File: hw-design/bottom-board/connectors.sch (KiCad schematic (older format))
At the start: 17 parts, among them J1 JACK_TRS_6PINS, J2 JACK_TRS_6PINS, J3 JACK_TRS_6PINS, J4 JACK_TRS_6PINS, J5 JACK_TRS_6PINS, J6 RJ45_LEDS, P5 BARREL_JACK, P6 HMI_POWER, P8 HMI_DATA, P9 SERIAL_DEBUG

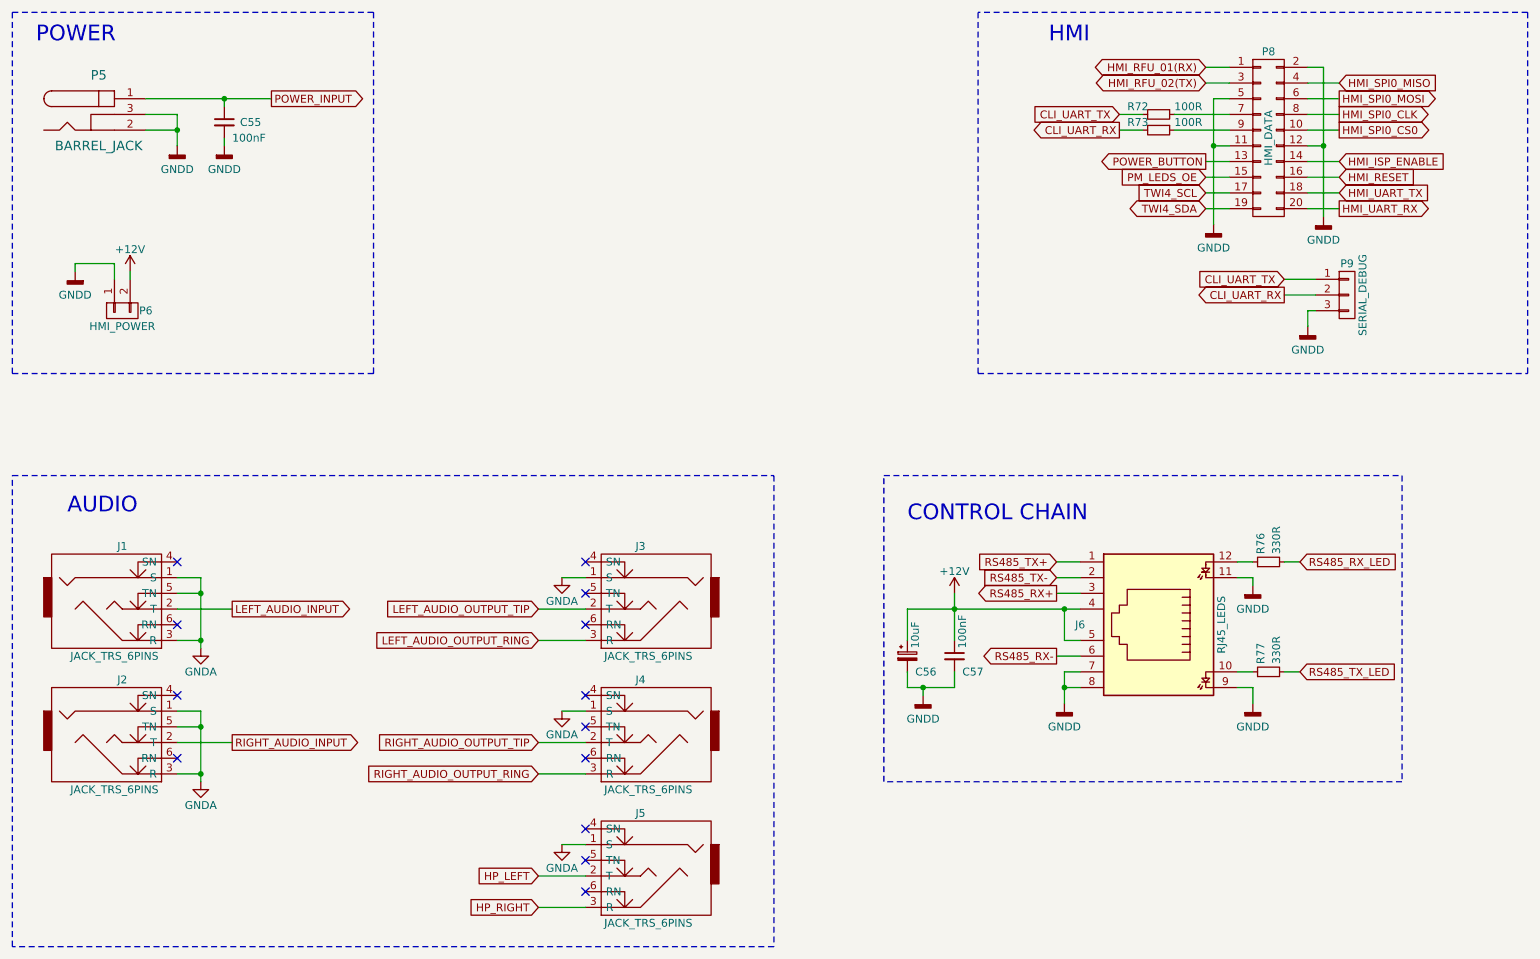
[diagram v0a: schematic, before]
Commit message: changed a bottomboard to a minimal HMI testing unit
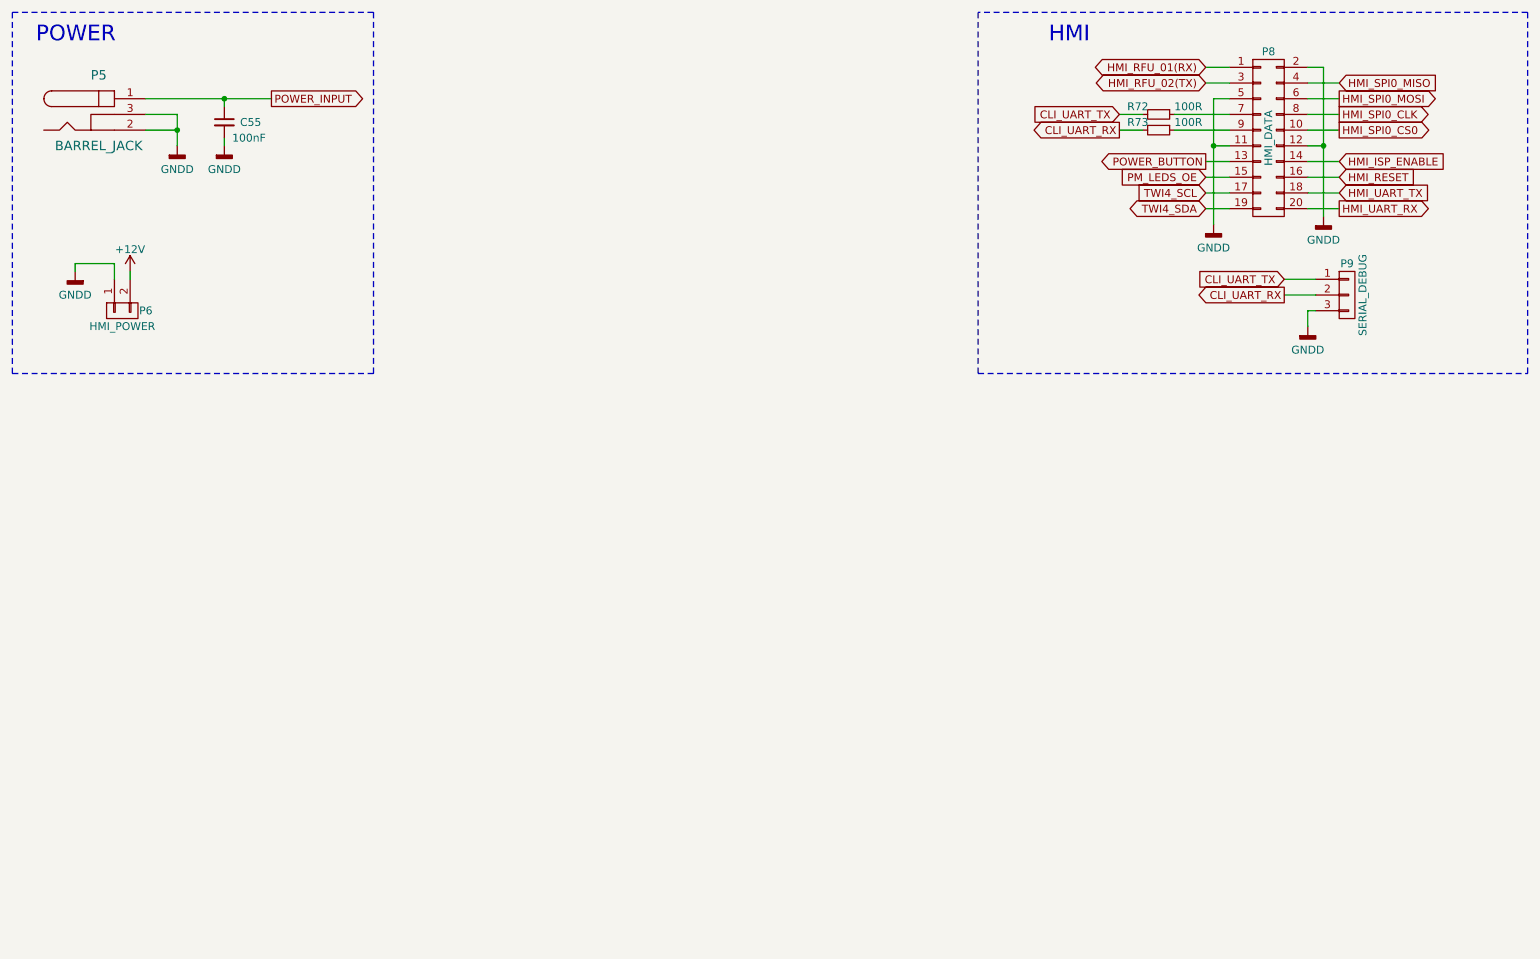
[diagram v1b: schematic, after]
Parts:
- removed C56: 10uF, Capacitors_SMD:c_elec_5x5.3, symbol bottom-board-rescue:CP_Small
- removed C57: 100nF, Capacitors_SMD:C_0603, symbol bottom-board-rescue:C_Small
- removed J1, J2, J3, J4, J5: JACK_TRS_6PINS, Connect:NMJ6HCD2, symbol bottom-board-rescue:JACK_TRS_6PINS
- removed J6: RJ45_LEDS, Connect:RJHSE538X, symbol bottom-board-rescue:RJ45_LEDS
- removed R76, R77: 330R, Resistors_SMD:R_0603, symbol bottom-board-rescue:R_Small
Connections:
- no-connect marks 13 -> 0
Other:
- note removed: "AUDIO"
- note removed: "CONTROL CHAIN"
